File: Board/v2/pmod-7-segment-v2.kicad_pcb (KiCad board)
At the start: 2 copper layers, 97.8 x 15.2 mm, 19 parts, among them J1 PMOD

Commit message: v2.0 routed and DRC ok, ready for mfg
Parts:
- removed MOUNTING_HOLE_3-2MM_M3 (x2): VAL**, Mounting_Holes_Local:MOUNTING_HOLE_3-2MM_M3
- LED1, LED2, LED3, LED4, LED5, LED6, LED7, LED8: footprint Kingbright:SA39-11 -> pmod-7-segment-v2:10pcs-1bit-1-bit-Common-Anode-Positive-Digital-Tube-0-36-0-36in-Red-LED-Digit
- moved LED8 19.9 mm to (169.3, 76.2)
- moved LED7 17.3 mm to (161.8, 76.2)
- moved LED6 14.6 mm to (154.3, 76.2)
- moved LED5 11.9 mm to (146.8, 76.2)
- moved LED4 9.29 mm to (139.3, 76.2)
- moved LED3 6.63 mm to (131.8, 76.2)
- moved LED2 4.17 mm to (124.1, 76.2)
- moved LED1 1.51 mm to (116.6, 76.2)
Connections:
- J1 pad 12: Net-(J1-Pad12) -> (no net)
- J1 pad 6: Net-(J1-Pad6) -> (no net)
- LED1 pad 6: Net-(LED1-Pad6) -> (no net)
- LED2 pad 6: Net-(LED2-Pad6) -> (no net)
- LED3 pad 6: Net-(LED3-Pad6) -> (no net)
- LED4 pad 6: Net-(LED4-Pad6) -> (no net)
- LED5 pad 6: Net-(LED5-Pad6) -> (no net)
- LED6 pad 6: Net-(LED6-Pad6) -> (no net)
- LED7 pad 6: Net-(LED7-Pad6) -> (no net)
- LED8 pad 6: Net-(LED8-Pad6) -> (no net)
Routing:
- net /S0: track 102.6 -> 72.0 mm
- net /S2: track 96.9 -> 68.5 mm, vias 3 -> 1
- net /S3: track 98.9 -> 71.8 mm, vias 2 -> 1
- net /S5: track 89.4 -> 65.4 mm
- net /S4: track 89.6 -> 66.4 mm
- net /S7: track 98.5 -> 76.9 mm
- net /S1: track 93.2 -> 72.8 mm
- net /S6: track 85.9 -> 66.3 mm
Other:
- board size 97.8 x 15.2 mm -> 71.4 x 15.2 mm
- board text added: "Pmod v2.0 7Segment"
- board text removed: "Pmod v1.0 7Segment"

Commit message: Silk fixes
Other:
- board text added: "pmod-7segment"
- board text added: "tom@tomk.in"
- board text added: "v2.0 August 2019"
- board text removed: "Pmod v2.0 7Segment"
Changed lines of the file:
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@@
   (general
     (thickness 1.6)
-    (drawings 9)
+    (drawings 11)
     (tracks 218)
     (zones 0)
@@
   )
   (setup
-    (last_trace_width 0.508)
+    (last_trace_width 0.254)
     (user_trace_width 0.508)
     (trace_clearance 0.1524)
@@
     )
   )
+  (gr_text "v2.0 August 2019" (at 116.586 76.2 90) (layer B.SilkS)
+    (effects (font (size 1.1 1.1) (thickness 0.2)))
+  )
+  (gr_text tom@tomk.in (at 111.252 76.2 90) (layer B.SilkS)
+    (effects (font (size 1.1 1.1) (thickness 0.2)))
+  )
   (gr_line (start 172.974 83.058) (end 172.974 69.342) (layer Edge.Cuts) (width 0.15))
   (gr_line (start 172.212 83.82) (end 102.362 83.82) (layer Edge.Cuts) (width 0.15))
@@
   (gr_arc (start 102.362 83.058) (end 101.6 83.058) (angle -90) (layer Edge.Cuts) (width 0.15))
   (gr_arc (start 102.362 69.342) (end 102.362 68.58) (angle -90) (layer Edge.Cuts) (width 0.15))
-  (gr_text "Pmod v2.0\n7Segment" (at 103.124 76.2 90) (layer F.SilkS)
-    (effects (font (size 0.8 0.9) (thickness 0.2)))
+  (gr_text pmod-7segment (at 103.124 76.2 90) (layer B.SilkS)
+    (effects (font (size 1.1 1.1) (thickness 0.2)))
   )
   (segment (start 107.95 72.39) (end 108.966 72.39) (width 0.508) (layer F.Cu) (net 1))

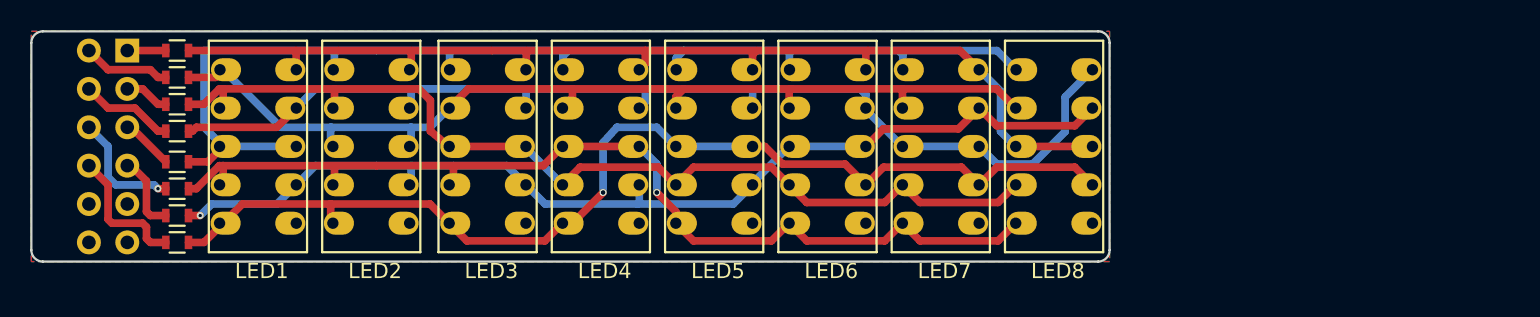
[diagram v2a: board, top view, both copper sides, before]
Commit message: pmod-7-segment-v2 : v2.1 as submitted to oshpark
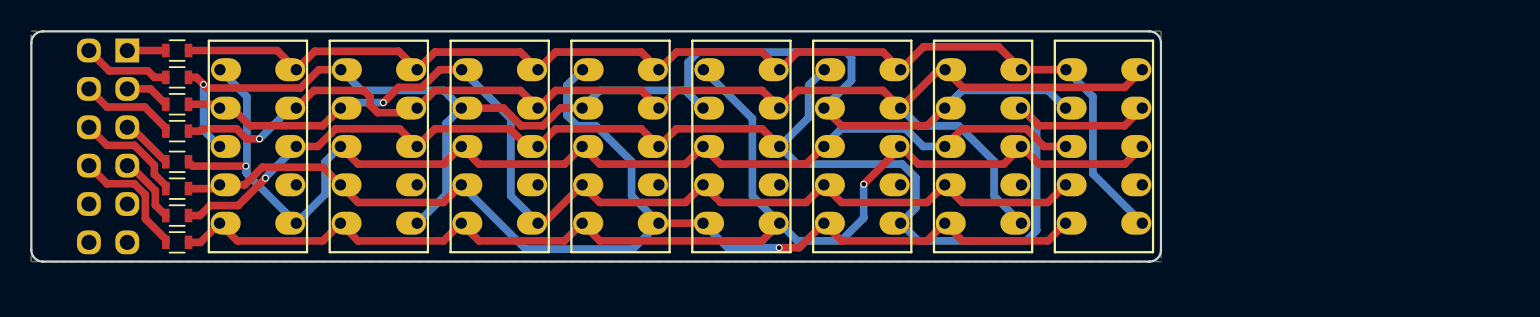
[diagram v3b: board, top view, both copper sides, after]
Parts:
- moved LED8 3.30 mm to (172.6, 76.2)
- moved LED7 2.80 mm to (164.6, 76.2)
- moved LED6 2.30 mm to (156.6, 76.2)
- moved LED5 1.80 mm to (148.6, 76.2)
- moved LED4 1.30 mm to (140.6, 76.2)
- moved LED3 0.80 mm to (132.6, 76.2)
- moved LED2 0.50 mm to (124.6, 76.2)
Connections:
- LED1 pad 1: /S6 -> /S7
- LED1 pad 3: /S7 -> /S6
- LED1 pad 6: (no net) -> /S7
- LED1 pad 7: /S2 -> (no net)
- LED1 pad 8: /S7 -> /S2
- LED2 pad 1: /S7 -> /S6
- LED2 pad 3: /S6 -> /S7
- LED2 pad 6: (no net) -> /S6
- LED2 pad 7: /S2 -> (no net)
- LED2 pad 8: /S6 -> /S2
- LED3 pad 1: /S7 -> /S5
- LED3 pad 3: /S5 -> /S7
- LED3 pad 6: (no net) -> /S5
- LED3 pad 7: /S2 -> (no net)
- LED3 pad 8: /S5 -> /S2
- LED4 pad 1: /S7 -> /S4
- LED4 pad 3: /S4 -> /S7
- LED4 pad 6: (no net) -> /S4
- LED4 pad 7: /S2 -> (no net)
- LED4 pad 8: /S4 -> /S2
- LED5 pad 1: /S7 -> /S3
- LED5 pad 3: /S3 -> /S7
- LED5 pad 6: (no net) -> /S3
- LED5 pad 7: /S2 -> (no net)
- LED5 pad 8: /S3 -> /S2
- LED6 pad 1: /S7 -> /S2
- LED6 pad 3: /S2 -> /S7
- LED6 pad 6: (no net) -> /S2
- LED6 pad 7: /S3 -> (no net)
- LED6 pad 8: /S2 -> /S3
- LED7 pad 1: /S7 -> /S1
- LED7 pad 3: /S1 -> /S7
- LED7 pad 6: (no net) -> /S1
- LED7 pad 7: /S3 -> (no net)
- LED7 pad 8: /S1 -> /S3
- LED8 pad 1: /S7 -> /S0
- LED8 pad 3: /S0 -> /S7
- LED8 pad 6: (no net) -> /S0
- LED8 pad 7: /S3 -> (no net)
- LED8 pad 8: /S0 -> /S3
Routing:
- net /S2: track 68.5 -> 91.8 mm
- net /S6: track 66.3 -> 87.9 mm, vias 0 -> 1
- net /S3: track 71.8 -> 86.1 mm
- net /S4: track 66.4 -> 79.7 mm
- net /S1: track 72.8 -> 84.6 mm, vias 0 -> 1
- net /S5: track 65.4 -> 72.3 mm, vias 0 -> 1
- net /S0: track 72.0 -> 77.0 mm
- net Net-(J1-Pad10): track 8.98 -> 8.25 mm
- net Net-(J1-Pad9): track 7.97 -> 7.24 mm, vias 1 -> 0
- net Net-(J1-Pad4): track 5.11 -> 4.48 mm
- net /S7: track 76.9 -> 76.8 mm, vias 0 -> 1
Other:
- board size 71.4 x 15.2 mm -> 74.8 x 15.2 mm
- board text added: "v2.1 Sept 2019"
- board text removed: "v2.0 August 2019"

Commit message: v2: renumber nets, fix SolderMaskClearance, fix copper pour isolation, v2.2
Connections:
- net /S0 renamed /IO1
- net /S1 renamed /IO6
- net /S2 renamed /IO4
- net /S3 renamed /IO8
- net /S4 renamed /IO7
- net /S5 renamed /IO2
- net /S6 renamed /IO5
- net /S7 renamed /IO3
- J1 pad 12: (no net) -> Net-(J1-Pad12)
- J1 pad 6: (no net) -> Net-(J1-Pad6)
- LED1 pad 7: (no net) -> Net-(LED1-Pad7)
- LED2 pad 7: (no net) -> Net-(LED2-Pad7)
- LED3 pad 7: (no net) -> Net-(LED3-Pad7)
- LED4 pad 7: (no net) -> Net-(LED4-Pad7)
- LED5 pad 7: (no net) -> Net-(LED5-Pad7)
- LED6 pad 7: (no net) -> Net-(LED6-Pad7)
- LED7 pad 7: (no net) -> Net-(LED7-Pad7)
- LED8 pad 7: (no net) -> Net-(LED8-Pad7)
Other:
- rule pad_to_mask_clearance: 0.2 -> 0
- board text added: "v2.2 Oct 2019"
- board text removed: "v2.1 Sept 2019"

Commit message: v2: update solder mask clearance to 0.0508
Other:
- rule pad_to_mask_clearance: 0 -> 0.0508
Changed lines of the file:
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@@
   (page A4)
   (layers
-    (0 F.Cu signal hide)
-    (31 B.Cu signal hide)
+    (0 F.Cu signal)
+    (31 B.Cu signal)
     (32 B.Adhes user)
-    (33 F.Adhes user hide)
+    (33 F.Adhes user)
     (34 B.Paste user)
     (35 F.Paste user)
@@
     (pad_size 3.2 3.2)
     (pad_drill 3.2)
-    (pad_to_mask_clearance 0)
+    (pad_to_mask_clearance 0.0508)
     (aux_axis_origin 0 0)
     (grid_origin 101.6 76.2)
